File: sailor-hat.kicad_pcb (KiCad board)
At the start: 2 copper layers, 65 x 56 mm, 103 parts, among them J1 Screw_Terminal_01x04, J2 Raspberry_Pi_2_3, J3 Conn_02x07_Counter_Clockwise, J4 Screw_Terminal_01x02, J5 Screw_Terminal_01x03, Q1 DMP3098L, SW1 SW_SPST, U1 ATtiny841-SSU, U2 TPS61022, U3 MD7133H, U4 DS3231MZ, U5 MP1584EN, U6 INA199A1DCKR, U7 MCP25625T-E_ML, U8 MCP25625T-E_ML, X1 S3D8.000000B20F30T

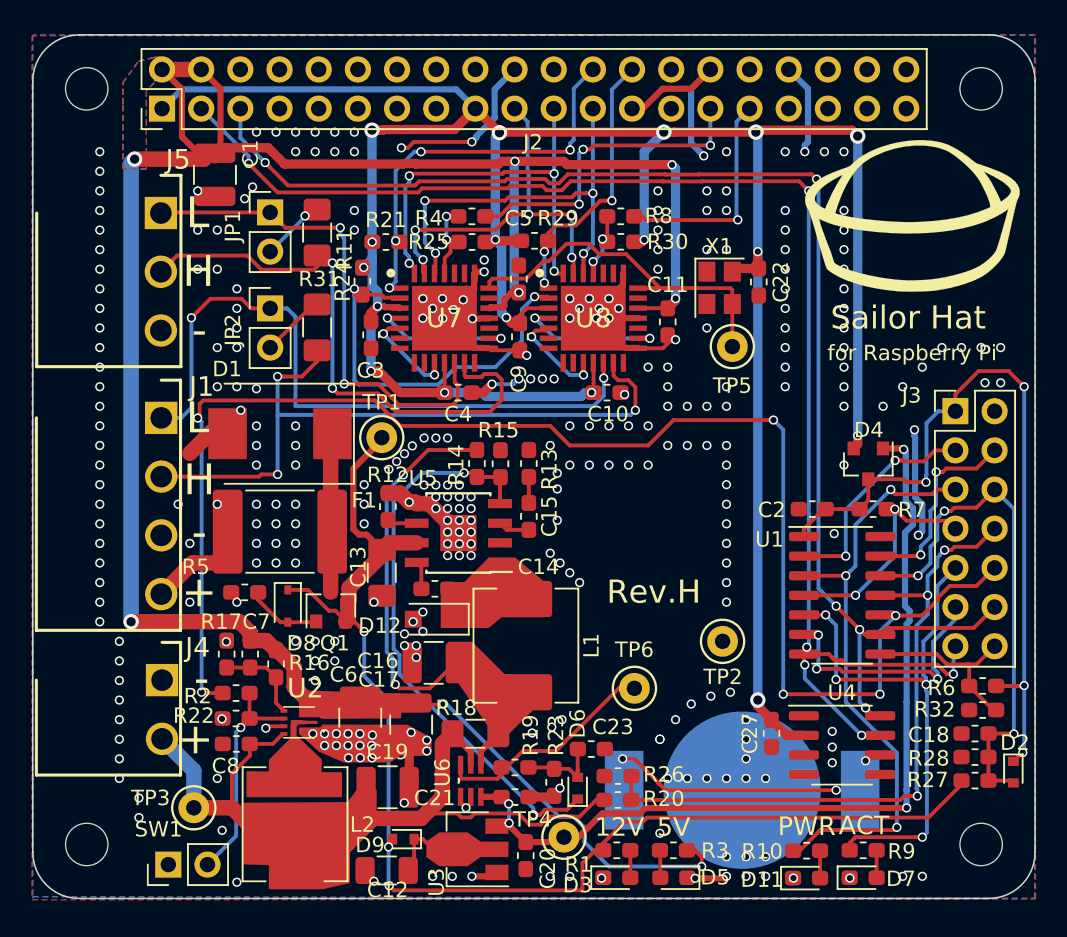
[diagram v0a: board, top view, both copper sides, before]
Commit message: Update parts according to JLCPCB availability
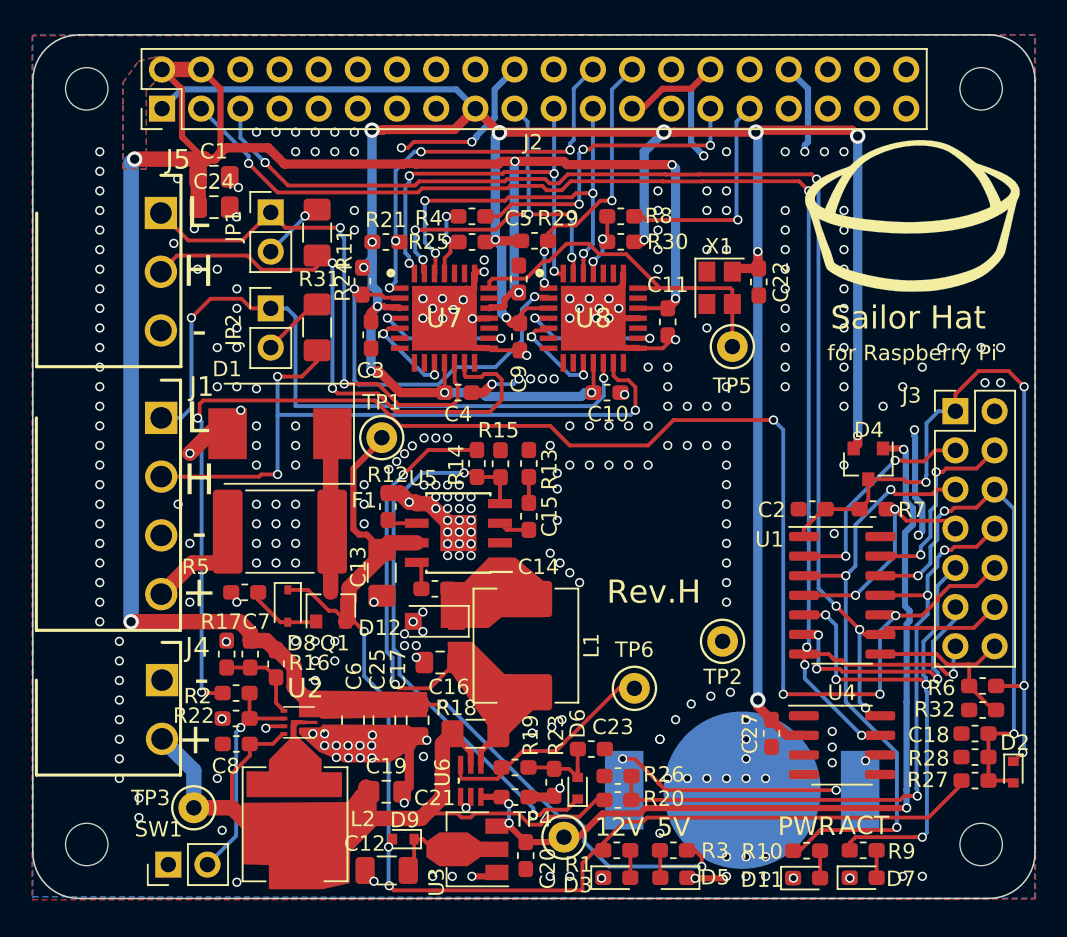
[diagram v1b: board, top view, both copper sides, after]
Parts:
- added C24: 22uF 6.3V, Capacitor_SMD:C_0805_2012Metric_Pad1.15x1.40mm_HandSolder, F.Cu at (31.9, 29.4)
- added C25: 22uF 6.3V, Capacitor_SMD:C_0805_2012Metric_Pad1.15x1.40mm_HandSolder, F.Cu at (43.0, 62.7)
- C1, C17, C6: value 47uF 10V -> 22uF 6.3V; footprint Capacitor_SMD:C_1210_3225Metric -> Capacitor_SMD:C_0805_2012Metric_Pad1.15x1.40mm_HandSolder
- C15: value 150pF -> 220pF
- C16: value 47uF 6V -> 22uF 6.3V; footprint Capacitor_SMD:C_1210_3225Metric -> Capacitor_SMD:C_0805_2012Metric_Pad1.15x1.40mm_HandSolder
- C19: value 47uF 6.3V -> 22uF 6.3V; footprint Capacitor_SMD:C_1210_3225Metric -> Capacitor_SMD:C_0805_2012Metric_Pad1.15x1.40mm_HandSolder
- C7: value 220p -> 220pF
- C8: value 100n -> 100nF
- D2, D6, D9: value RB521S-30 -> SDM10U45-7
- R13: value 54.9k -> 56k
- R14: value 93k -> 82k
- R15: value 40.2k -> 36k
- U3: value MD7133H -> HT7533-1
- X1: value S3D8.000000B20F30T -> SiT8008AI-22-33E-8.000000D
- moved C17 0.51 mm to (45.1, 62.7)
- moved C6 0.50 mm to (41.0, 62.7)
- moved C16 0.42 mm to (46.6, 58.9)
- moved C19 0.31 mm to (43.1, 67.3)
- moved C1 0.14 mm to (31.9, 27.4), turned to 0 degrees
- moved D12 0.14 mm to (46.3, 56.3)
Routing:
- net 5V: track 159.7 -> 162.8 mm
- net /CAN0_L: track 32.8 -> 34.3 mm
- net GND: vias 318 -> 316
- net +12V: vias 1 -> 0

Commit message: Isolated CAN bus implementation
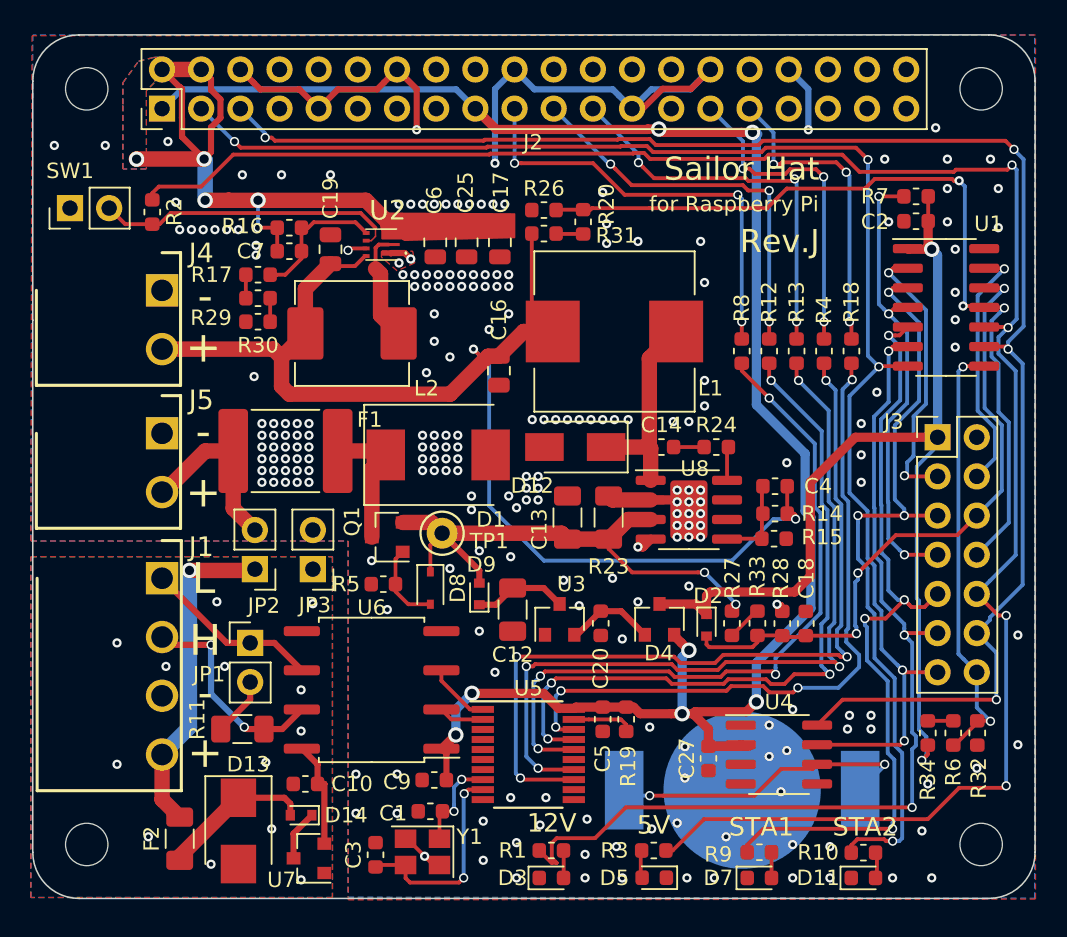
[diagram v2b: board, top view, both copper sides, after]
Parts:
- removed C11, C21, C22, C8: 100nF, Capacitor_SMD:C_0603_1608Metric_Pad1.05x0.95mm_HandSolder
- removed C15: 220pF, Capacitor_SMD:C_0603_1608Metric_Pad1.05x0.95mm_HandSolder
- removed C23: 470nF, Capacitor_SMD:C_0603_1608Metric_Pad1.05x0.95mm_HandSolder
- removed C24: 22uF 6.3V, Capacitor_SMD:C_0805_2012Metric_Pad1.15x1.40mm_HandSolder
- removed D6: SDM10U45-7, Diode_SMD:D_SOD-523
- removed the G*** at (77.2, 30.0)
- removed R21, R25: 10k, Resistor_SMD:R_0603_1608Metric_Pad1.05x0.95mm_HandSolder
- removed R22: 100k, Resistor_SMD:R_0603_1608Metric_Pad1.05x0.95mm_HandSolder
- removed TP2: GND, TestPoint:TestPoint_Keystone_5000-5004_Miniature
- removed TP3: Vcap, TestPoint:TestPoint_Keystone_5000-5004_Miniature
- removed TP4: REG3.3V, TestPoint:TestPoint_Keystone_5000-5004_Miniature
- removed TP5: OSC, TestPoint:TestPoint_Keystone_5000-5004_Miniature
- removed TP6: CSA Out, TestPoint:TestPoint_Keystone_5000-5004_Miniature
- removed X1: SiT8008AI-22-33E-8.000000D, Oscillator:Oscillator_SMD_Abracon_ASE-4Pin_3.2x2.5mm
- added D13: SMBJ20CA, Diode_SMD:D_SMB, F.Cu at (33.5, 69.8)
- added D14: SDM10U45-7, Diode_SMD:D_SOD-523, F.Cu at (37.6, 68.8)
- added F2: SMD1206P010TF, Fuse:Fuse_1206_3216Metric, F.Cu at (29.7, 70.4)
- added JP3: Term, Connector_PinHeader_2.54mm:PinHeader_1x02_P2.54mm_Vertical, F.Cu at (38.4, 52.9)
- added R33: 100k, Resistor_SMD:R_0603_1608Metric, F.Cu at (67.2, 56.4)
- added R34: 100k, Resistor_SMD:R_0603_1608Metric, F.Cu at (78.2, 63.5)
- added Y1: TAXM8M4RFDCET2T, Crystal:Crystal_SMD_3225-4Pin_3.2x2.5mm, F.Cu at (45.5, 71.2)
- C1: value 22uF 6.3V -> 22p; footprint Capacitor_SMD:C_0805_2012Metric_Pad1.15x1.40mm_HandSolder -> Capacitor_SMD:C_0603_1608Metric
- C10, C14, C18, C2, C20, C27, C5, C7, C9: footprint Capacitor_SMD:C_0603_1608Metric_Pad1.05x0.95mm_HandSolder -> Capacitor_SMD:C_0603_1608Metric
- C13: footprint Capacitor_SMD:C_1206_3216Metric_Pad1.42x1.75mm_HandSolder -> Capacitor_SMD:C_1206_3216Metric
- C16, C17, C19, C25, C6: footprint Capacitor_SMD:C_0805_2012Metric_Pad1.15x1.40mm_HandSolder -> Capacitor_SMD:C_0805_2012Metric
- C3: value 100nF -> 22p; footprint Capacitor_SMD:C_0603_1608Metric_Pad1.05x0.95mm_HandSolder -> Capacitor_SMD:C_0603_1608Metric
- C4: value 100nF -> 22pF; footprint Capacitor_SMD:C_0603_1608Metric_Pad1.05x0.95mm_HandSolder -> Capacitor_SMD:C_0603_1608Metric
- D1: value 5.0SMDJ16CA -> 5.0SMDJ20CA
- D11, D5, D7: footprint LED_SMD:LED_0603_1608Metric_Pad1.05x0.95mm_HandSolder -> LED_SMD:LED_0603_1608Metric
- D12: value DS34W -> SS54F; footprint Diode_SMD:D_SOD-123F -> Diode_SMD:D_SMA
- D3: value RLED -> GLED; footprint LED_SMD:LED_0603_1608Metric_Pad1.05x0.95mm_HandSolder -> LED_SMD:LED_0603_1608Metric
- F1: value 2920L110/60MR (1.1A) -> ASMD2920-185
- J5: value Screw_Terminal_01x03 -> Screw_Terminal_01x02; footprint custom:TerminalBlock_WJ15EDGRC-3.81-3P -> custom:TerminalBlock_WJ15EDGRC-3.81-2P
- L1: value 4.7uH 3.5A -> SMMS1040-100M; footprint Inductor_SMD:L_Abracon_ASPI-0630LR -> Inductor_SMD:L_Wuerth_HCI-1040
- R1: value 4.7k -> 2.2k; footprint Resistor_SMD:R_0603_1608Metric_Pad1.05x0.95mm_HandSolder -> Resistor_SMD:R_0603_1608Metric
- R10, R9: value 1.5k -> 2.2k; footprint Resistor_SMD:R_0603_1608Metric_Pad1.05x0.95mm_HandSolder -> Resistor_SMD:R_0603_1608Metric
- R11: footprint Resistor_SMD:R_1206_3216Metric_Pad1.42x1.75mm_HandSolder -> Resistor_SMD:R_1206_3216Metric
- R12: value 200k -> 0; footprint Resistor_SMD:R_0603_1608Metric_Pad1.05x0.95mm_HandSolder -> Resistor_SMD:R_0603_1608Metric
- R13: value 56k -> 0; footprint Resistor_SMD:R_0603_1608Metric_Pad1.05x0.95mm_HandSolder -> Resistor_SMD:R_0603_1608Metric
- R14: value 82k -> 300k; footprint Resistor_SMD:R_0603_1608Metric_Pad1.05x0.95mm_HandSolder -> Resistor_SMD:R_0603_1608Metric
- R15: value 36k -> 133k; footprint Resistor_SMD:R_0603_1608Metric_Pad1.05x0.95mm_HandSolder -> Resistor_SMD:R_0603_1608Metric
- R16: value 330k -> 300k; footprint Resistor_SMD:R_0603_1608Metric_Pad1.05x0.95mm_HandSolder -> Resistor_SMD:R_0603_1608Metric
- R17: value 43k -> 13k; footprint Resistor_SMD:R_0603_1608Metric_Pad1.05x0.95mm_HandSolder -> Resistor_SMD:R_0603_1608Metric
- R18: value 20m -> 0; footprint Resistor_SMD:R_1206_3216Metric_Pad1.42x1.75mm_HandSolder -> Resistor_SMD:R_0603_1608Metric
- R19: value 9.1k -> 10k; footprint Resistor_SMD:R_0603_1608Metric_Pad1.05x0.95mm_HandSolder -> Resistor_SMD:R_0603_1608Metric
- R2, R20, R27, R3, R4, R5, R7, R8: footprint Resistor_SMD:R_0603_1608Metric_Pad1.05x0.95mm_HandSolder -> Resistor_SMD:R_0603_1608Metric
- R23: value 4.7k -> 20m; footprint Resistor_SMD:R_0603_1608Metric_Pad1.05x0.95mm_HandSolder -> Resistor_SMD:R_1206_3216Metric
- R24: value 10k -> 5.1; footprint Resistor_SMD:R_0603_1608Metric_Pad1.05x0.95mm_HandSolder -> Resistor_SMD:R_0603_1608Metric
- R26: value 68k -> 133k; footprint Resistor_SMD:R_0603_1608Metric_Pad1.05x0.95mm_HandSolder -> Resistor_SMD:R_0603_1608Metric
- R28: value 7.5k -> 13k; footprint Resistor_SMD:R_0603_1608Metric_Pad1.05x0.95mm_HandSolder -> Resistor_SMD:R_0603_1608Metric
- R29, R30: value 10k -> 13k; footprint Resistor_SMD:R_0603_1608Metric_Pad1.05x0.95mm_HandSolder -> Resistor_SMD:R_0603_1608Metric
- R31: value 120R -> 100k; footprint Resistor_SMD:R_1206_3216Metric_Pad1.42x1.75mm_HandSolder -> Resistor_SMD:R_0603_1608Metric
- R32: value 10k -> 100k; footprint Resistor_SMD:R_0603_1608Metric_Pad1.05x0.95mm_HandSolder -> Resistor_SMD:R_0603_1608Metric
- R6: value inf -> 100k; footprint Resistor_SMD:R_0603_1608Metric_Pad1.05x0.95mm_HandSolder -> Resistor_SMD:R_0603_1608Metric
- U3: value HT7533-1 -> H7533-H#; footprint Package_TO_SOT_SMD:SOT-89-3 -> Package_TO_SOT_SMD:SOT-23
- U5: value MP1584EN -> MCP2515-xST; footprint Package_SO:SOIC-8-1EP_3.9x4.9mm_P1.27mm_EP2.35x2.35mm -> Package_SO:TSSOP-20_4.4x6.5mm_P0.65mm
- U6: value INA199A1DCKR -> ISO1050DUB; footprint custom:SOT65P210X110-6N -> Package_SO:SOP-8_6.62x9.15mm_P2.54mm
- U7: value MCP25625T-E_ML -> H7550-H#; footprint custom:QFN65P600X600X100-29M-D -> Package_TO_SOT_SMD:SOT-23
- U8: value MCP25625T-E_ML -> TX4138; footprint custom:QFN65P600X600X100-29M-D -> Package_SO:SOIC-8-1EP_3.9x4.9mm_P1.27mm_EP2.41x3.81mm
- moved C1 43.5 mm to (46.0, 68.6), turned to 180 degrees
- moved SW1 43.0 mm to (22.6, 29.5)
- moved R20 37.6 mm to (55.9, 30.4), turned to 90 degrees
- moved R26 37.0 mm to (53.3, 29.6)
- moved U7 36.1 mm to (38.1, 71.6), turned to 180 degrees
- moved C19 35.4 mm to (39.5, 32.1), turned to 90 degrees
- moved R18 34.8 mm to (73.3, 38.7), turned to 90 degrees
- moved C3 33.7 mm to (42.4, 71.4), turned to 90 degrees
- moved R11 32.6 mm to (33.8, 63.2), turned to 0 degrees
- moved L2 32.0 mm to (40.9, 37.6), turned to 0 degrees
- moved C10 32.0 mm to (37.9, 66.8), turned to 180 degrees
- moved R2 31.7 mm to (27.9, 29.7), turned to 270 degrees
- moved C17 31.4 mm to (50.5, 31.7)
- moved C25 31.4 mm to (48.3, 31.7)
- moved C6 31.4 mm to (46.3, 31.7)
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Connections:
- C1 pad 1: 5V -> /CANbus interface/OSC2
- C10 pad 1: 3.3V -> /CANbus interface/CAN_5V
- C10 pad 2: GND -> /CAN0_GND
- C13 pad 1: /inv_Sense_Vcc/12V_prot -> /Control MCU/12V_prot
- C14 pad 2: /Buck converter/BST -> Net-(C14-Pad2)
- C16 pad 1: /Buck converter/Vout -> /Vcap
- C3 pad 1: 3.3V -> /CANbus interface/OSC1
- C4 pad 1: 3.3V -> /Vcap
- C4 pad 2: GND -> /Buck converter/FB
- C5 pad 1: 5V -> 3.3V
- D8 pad 1: /inv_Sense_Vcc/12V_prot -> /Control MCU/12V_prot
- D9 pad 2: /inv_Sense_Vcc/12V_prot -> /Control MCU/12V_prot
- J1 pad 1: /CAN1_L -> /CAN0_L
- J1 pad 2: /CAN1_H -> /CAN0_H
- J1 pad 3: GND -> /CAN0_GND
- J1 pad 4: +12V -> /CAN0_12V
- J2 pad 19: /SI -> /GPIO10
- J2 pad 21: /SO -> /GPIO9
- J2 pad 23: /SCK -> /GPIO11
- J2 pad 24: /CS0 -> (no net)
- J2 pad 26: /CS1 -> (no net)
- J3 pad 6: /PA7 -> /ATT_LED2
- J5 pad 1: /CAN0_L -> GND
- J5 pad 2: /CAN0_H -> +12V
- JP2 pad 1: /CAN1_L -> /CAN0_12V
- JP2 pad 2: Net-(JP2-Pad2) -> +12V
- L1 pad 2: /Buck converter/Vout -> /Vcap
- Q1 pad 2: /inv_Sense_Vcc/12V_prot -> /Control MCU/12V_prot
- R1 pad 1: /inv_Sense_Vcc/12V_prot -> /ATT_LED2
- R12 pad 1: /Buck converter/FREQ -> /SO
- R12 pad 2: GND -> /GPIO9
- R13 pad 1: Net-(C15-Pad2) -> /SCK
- R13 pad 2: GND -> /GPIO11
- R14 pad 1: /Buck converter/Vout -> /Vcap
- R17 pad 2: GND -> Net-(R17-Pad2)
- R18 pad 1: /Vcap -> /CS0
- R18 pad 2: /Buck converter/Vout -> /GPIO6
- R19 pad 1: /Buck converter/CSAOUT -> 3.3V
- R19 pad 2: /Buck converter/CODIV -> /CANbus interface/RST
- R20 pad 1: /Vcap -> Net-(R20-Pad1)
- R23 pad 1: /Buck converter/CODIV -> /Buck converter/ILIM
- R23 pad 2: GND -> /Control MCU/12V_prot
- R24 pad 1: /CANbus interface/~RESET -> Net-(C14-Pad2)
- R24 pad 2: 3.3V -> /Buck converter/BS
- R27 pad 1: /inv_Sense_Vcc/12V_prot -> /Control MCU/12V_prot
- R27 pad 2: /V12s -> Net-(R27-Pad2)
- R29 pad 1: 3.3V -> Net-(R17-Pad2)
- R29 pad 2: /CS1 -> Net-(R29-Pad2)
- R3 pad 1: 5V -> /EN5V
- R30 pad 1: 3.3V -> Net-(R29-Pad2)
- R30 pad 2: /INT1 -> GND
- R31 pad 1: Net-(JP2-Pad2) -> /Vcap
- R31 pad 2: /CAN1_H -> Net-(R20-Pad1)
- R6 pad 1: /ATT_Vcc -> Net-(R34-Pad2)
- R8 pad 1: /INT1 -> /SI
- R8 pad 2: /GPIO6 -> /GPIO10
- TP1 pad 1: /inv_Sense_Vcc/12V_prot -> /Control MCU/12V_prot
- U1 pad 6: /PA7 -> /ATT_LED2
- U3 pad 2: Net-(C12-Pad1) -> REG3.3V
- U3 pad 3: REG3.3V -> Net-(C12-Pad1)
- U5 pad 1: /Buck converter/SW -> /CANbus interface/CAN_TX
- U5 pad 2: (no net) -> /CANbus interface/CAN_RX
- U5 pad 3: /Buck converter/COMP -> (no net)
- U5 pad 4: /Buck converter/FB -> (no net)
- U5 pad 5: GND -> (no net)
- U5 pad 6: /Buck converter/FREQ -> (no net)
- U5 pad 7: /inv_Sense_Vcc/12V_prot -> (no net)
- U5 pad 8: /Buck converter/BST -> /CANbus interface/OSC2
- U5 pad 9: GND -> /CANbus interface/OSC1
- U6 pad 1: GND -> 3.3V
- U6 pad 2: GND -> /CANbus interface/CAN_RX
- U6 pad 3: REG3.3V -> /CANbus interface/CAN_TX
- U6 pad 4: /Buck converter/Vout -> GND
- U6 pad 5: /Vcap -> /CAN0_GND
- U6 pad 6: /Buck converter/CSAOUT -> /CAN0_L
- U7 pad 1: /CS0 -> /CAN0_GND
- U7 pad 2: /CANbus interface/~RESET -> /CANbus interface/CAN_5V
- U7 pad 3: 3.3V -> /CANbus interface/CAN12V_prot
- U8 pad 1: /CS1 -> /Buck converter/SW
- U8 pad 2: /CANbus interface/~RESET -> /Buck converter/ILIM
- U8 pad 3: 3.3V -> /Control MCU/12V_prot
- U8 pad 4: Net-(U8-Pad16) -> GND
- U8 pad 5: Net-(U8-Pad10) -> /Buck converter/FB
- U8 pad 8: (no net) -> /Buck converter/BS
- U8 pad 9: (no net) -> /Buck converter/ILIM
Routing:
- net 5V: track 162.8 -> 50.6 mm, vias 8 -> 5
- net /inv_Sense_Vcc/12V_prot: track 82.7 -> 0.00 mm, vias 3 -> 0
- net 3.3V: track 183.9 -> 119.6 mm, vias 17 -> 7
- net /ATT_LED2: track 0.00 -> 62.0 mm, vias 0 -> 3
- net REG3.3V: track 58.0 -> 5.85 mm, vias 4 -> 0
- net /INT0: track 5.37 -> 53.3 mm, vias 2 -> 4
- net /CAN1_H: track 45.0 -> 0.00 mm, vias 3 -> 0
- net /CAN1_L: track 44.0 -> 0.00 mm, vias 2 -> 0
- net GND: track 96.7 -> 58.0 mm, vias 316 -> 210
- net /Buck converter/Vout: track 36.1 -> 0.00 mm, vias 2 -> 0
- net /Control MCU/12V_prot: track 0.00 -> 35.2 mm, vias 0 -> 2
- net /Buck converter/FB: track 36.9 -> 5.70 mm, vias 2 -> 0
- net /EN5V: track 98.0 -> 127.1 mm, vias 6 -> 4
- net /Vcap: track 55.2 -> 83.9 mm, vias 0 -> 2
- net /GPIO10: track 0.00 -> 28.3 mm, vias 0 -> 3
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- added copper zone on B.Cu, net /CAN0_GND
- added copper zone on F.Cu, net /CAN0_GND
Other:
- board text added: "CAN"
- board text added: "Rev.J"
- board text added: "STA1"
- board text added: "STA2"
- board text removed: "ACT"
- board text removed: "CAN0"
- board text removed: "CAN1"
- board text removed: "Rev.H"

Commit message: Optimize PCB layout; add missing filter caps
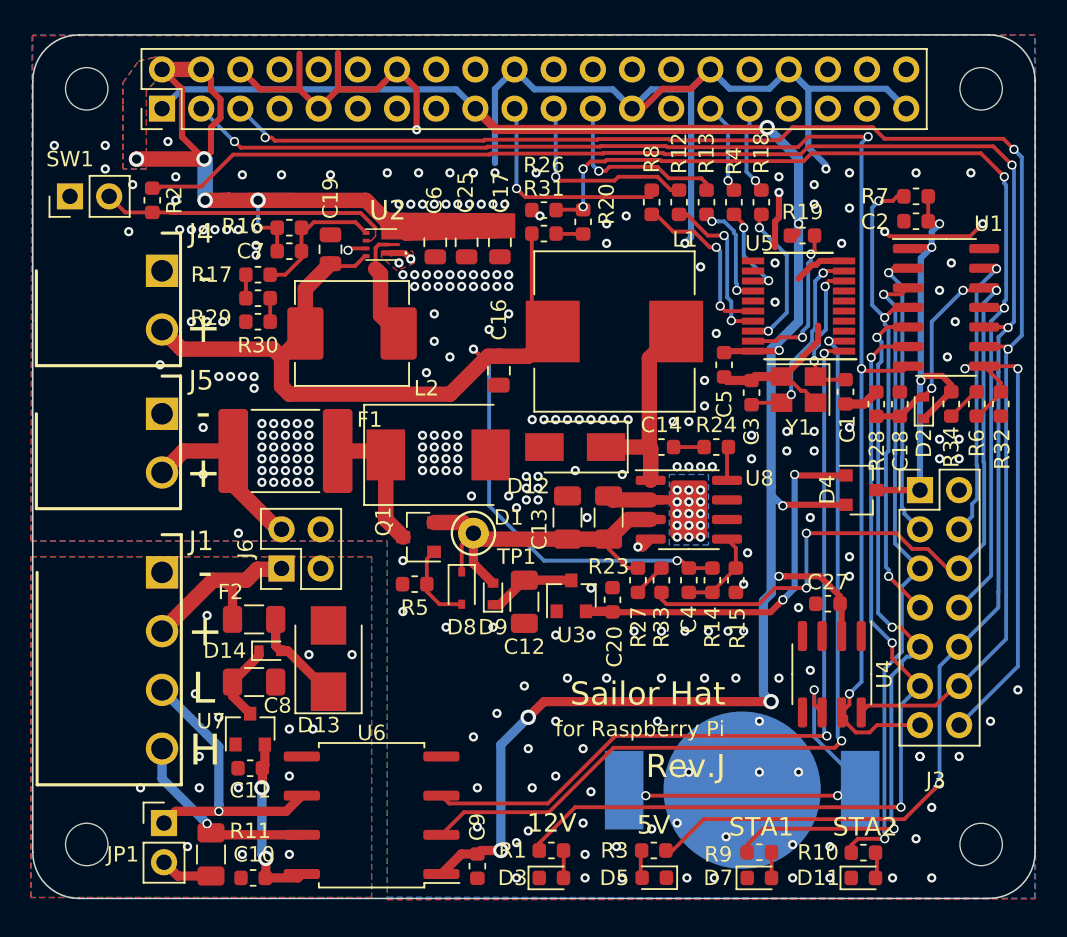
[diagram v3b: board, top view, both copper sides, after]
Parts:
- removed JP2, JP3: Term, Connector_PinHeader_2.54mm:PinHeader_1x02_P2.54mm_Vertical
- removed the REF** at (52.6, 33.0)
- added C11: 2.2uF 16V, Capacitor_SMD:C_0603_1608Metric, F.Cu at (34.3, 65.8)
- added C8: 2.2uF 50V, Capacitor_SMD:C_1206_3216Metric, F.Cu at (34.5, 60.2)
- added J6: Conn_02x02_Odd_Even, Connector_PinHeader_2.54mm:PinHeader_2x02_P2.54mm_Vertical, F.Cu at (36.3, 52.8)
- moved C3 38.6 mm to (66.8, 41.4)
- moved Y1 38.6 mm to (69.8, 41.2)
- moved C1 38.3 mm to (72.9, 41.4), turned to 270 degrees
- moved U5 34.0 mm to (69.8, 35.8), turned to 180 degrees
- moved R19 33.4 mm to (70.1, 31.2), turned to 0 degrees
- moved C5 24.3 mm to (65.0, 39.6)
- moved R32 21.4 mm to (83.0, 42.2)
- moved R34 21.4 mm to (79.8, 42.2), turned to 270 degrees
- moved R6 21.4 mm to (81.4, 42.2)
- moved D2 19.9 mm to (78.0, 42.4), turned to 90 degrees
- moved D4 15.5 mm to (73.9, 47.8), turned to 0 degrees
- moved R28 15.5 mm to (74.9, 42.2)
- moved C18 15.5 mm to (76.4, 42.2)
- moved G*** 15.3 mm to (45.2, 69.6)
- moved REF** 15.3 mm to (45.2, 58.4)
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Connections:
- J1 pad 1: /CAN0_L -> /CAN0_GND
- J1 pad 2: /CAN0_H -> /CAN0_12V
- J1 pad 3: /CAN0_GND -> /CAN0_L
- J1 pad 4: /CAN0_12V -> /CAN0_H
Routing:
- net GND: track 58.0 -> 115.5 mm, vias 210 -> 256
- net /CANbus interface/CAN_RX: track 2.95 -> 55.7 mm, vias 0 -> 2
- net /CANbus interface/CAN_TX: track 4.13 -> 53.3 mm, vias 0 -> 2
- net /INT0: track 53.3 -> 6.26 mm, vias 4 -> 2
- net /SCK: track 51.3 -> 7.28 mm, vias 4 -> 2
- net /ATT_Vcc: track 67.8 -> 29.9 mm, vias 2 -> 3
- net /SO: track 46.6 -> 10.6 mm, vias 4 -> 2
- net /SI: track 46.8 -> 11.5 mm, vias 4 -> 2
- net /CS0: track 44.6 -> 9.84 mm, vias 4 -> 2
- net REG3.3V: track 5.85 -> 25.1 mm, vias 0 -> 2
- net /V12s: track 42.0 -> 57.8 mm, vias 3 -> 5
- net /GPIO5: track 21.0 -> 5.92 mm, vias 3 -> 1
- net /GPIO6: track 20.2 -> 5.77 mm, vias 3 -> 1
- net /GPIO10: track 28.3 -> 14.7 mm, vias 3 -> 1
- net /GPIO11: track 25.8 -> 12.2 mm, vias 3 -> 1
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- added copper zone on B.Cu, net /Buck converter/ILIM

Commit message: Parts updated to match JLCPCB availability
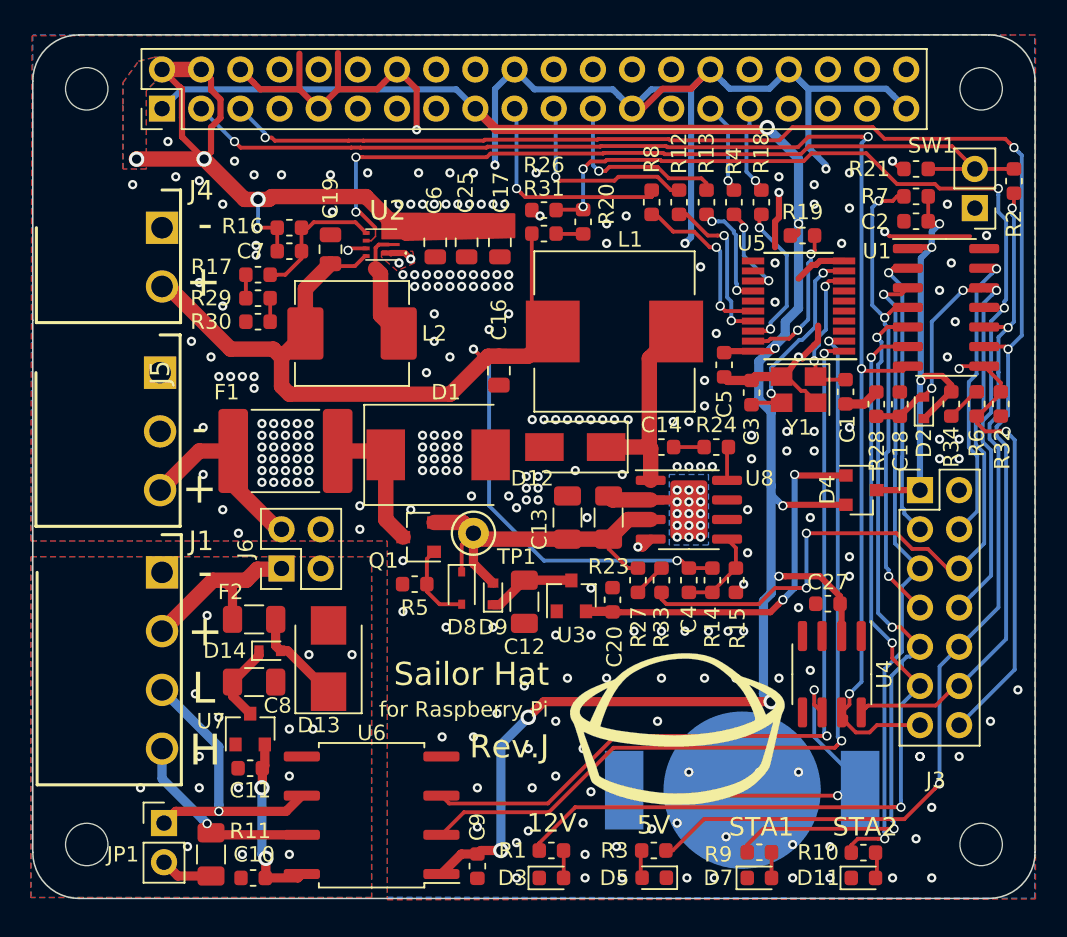
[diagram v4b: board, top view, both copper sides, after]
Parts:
- added G***: LOGO, custom:sailor-hat-logo, F.Cu at (62.0, 63.2)
- added R21: 100k, Resistor_SMD:R_0603_1608Metric, F.Cu at (77.5, 26.9)
- C1, C3: value 22p -> 22pF
- D14, D2, D9: value SDM10U45-7 -> PSBD521S-40
- J5: value Screw_Terminal_01x02 -> Screw_Terminal_01x03; footprint custom:TerminalBlock_WJ15EDGRC-3.81-2P -> custom:TerminalBlock_WJ15EDGRC-3.81-3P
- L1: value SMMS1040-100M -> MWSA1004-150MT
- L2: value 1uH -> MWSA0603-1R0MT
- R15, R26: value 133k -> 130k
- Y1: value TAXM8M4RFDCET2T -> 1C208000BC0R
- moved SW1 58.7 mm to (81.3, 29.5), turned to 180 degrees
- moved R2 55.9 mm to (83.8, 27.7), turned to 90 degrees
- moved J4 2.79 mm to (28.6, 30.7)
- moved J5 2.67 mm to (28.4, 40.1)
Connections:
- net Net-(R2-Pad2) renamed /Boost converter/ENIN
- J5 pad 2: +12V -> GND
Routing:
- net /EN5V: track 120.7 -> 62.0 mm
- net /Boost converter/ENIN: track 19.9 -> 53.1 mm, vias 0 -> 2
- net /PA5: track 32.8 -> 29.5 mm
- net 5V: track 50.6 -> 49.1 mm, vias 5 -> 4
- net /Vcap: track 75.5 -> 76.7 mm
- net /CANbus interface/OSC1: track 13.0 -> 13.7 mm
- net +12V: track 11.5 -> 12.1 mm
- net /SCL: track 97.6 -> 98.2 mm
